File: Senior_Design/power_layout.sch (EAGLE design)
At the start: 110 parts, among them J1 AU-Y1008-2, J2 U.FL-R-SMT-1(01), J3 U.FL-R-SMT-1(01), T1 BCX70SMD, T2 BCX70SMD, U1 SIM7000E, U2 TUSB2046BVFR, U3 MAX3373EEKA+T, U4 TPS2044BDR, X1 332-04

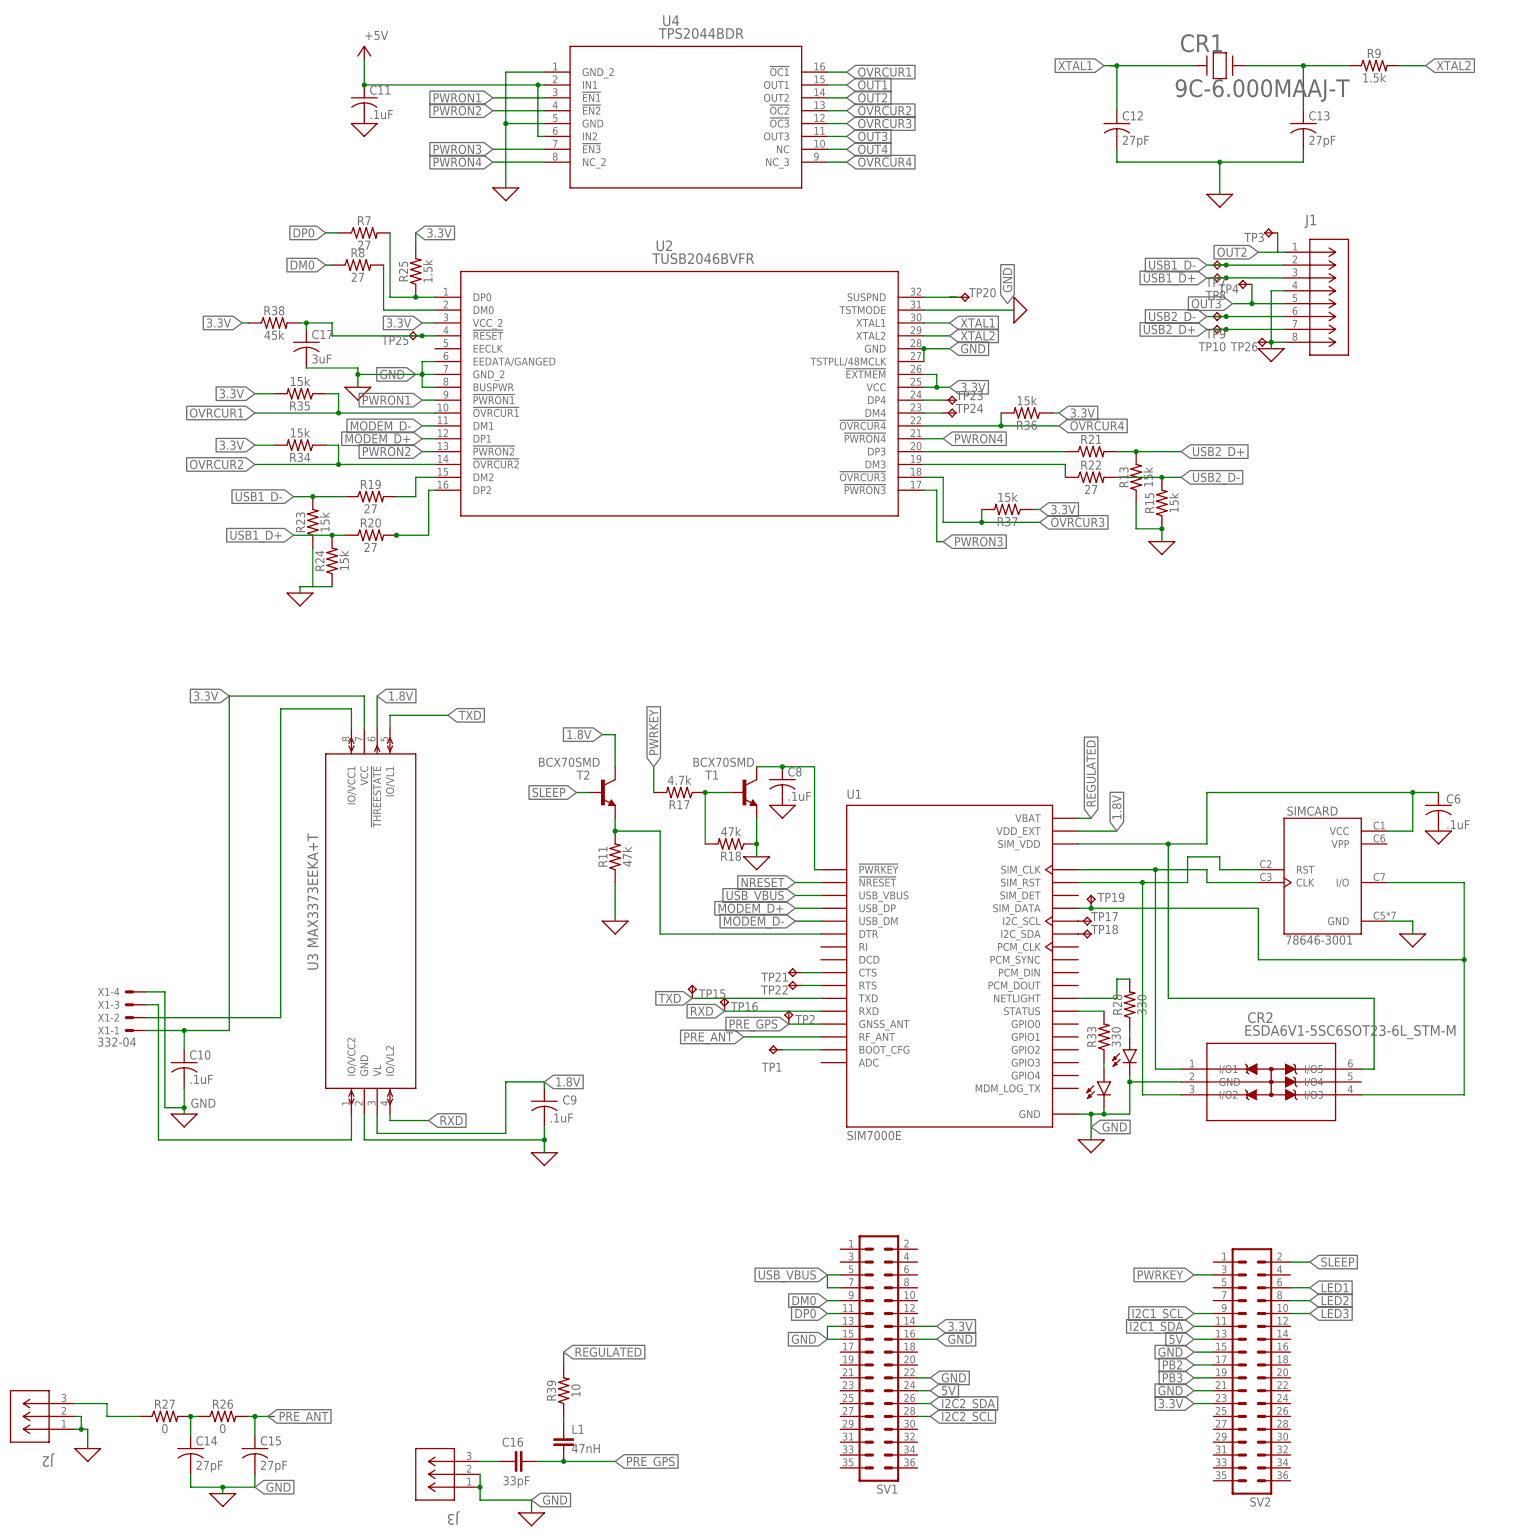
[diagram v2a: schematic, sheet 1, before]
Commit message: Add files via upload
This push includes the changes from Dr Pitts' Review and is THE Beta Board for purchasing.
-Cam files are processed in the folder "Beta Spin"
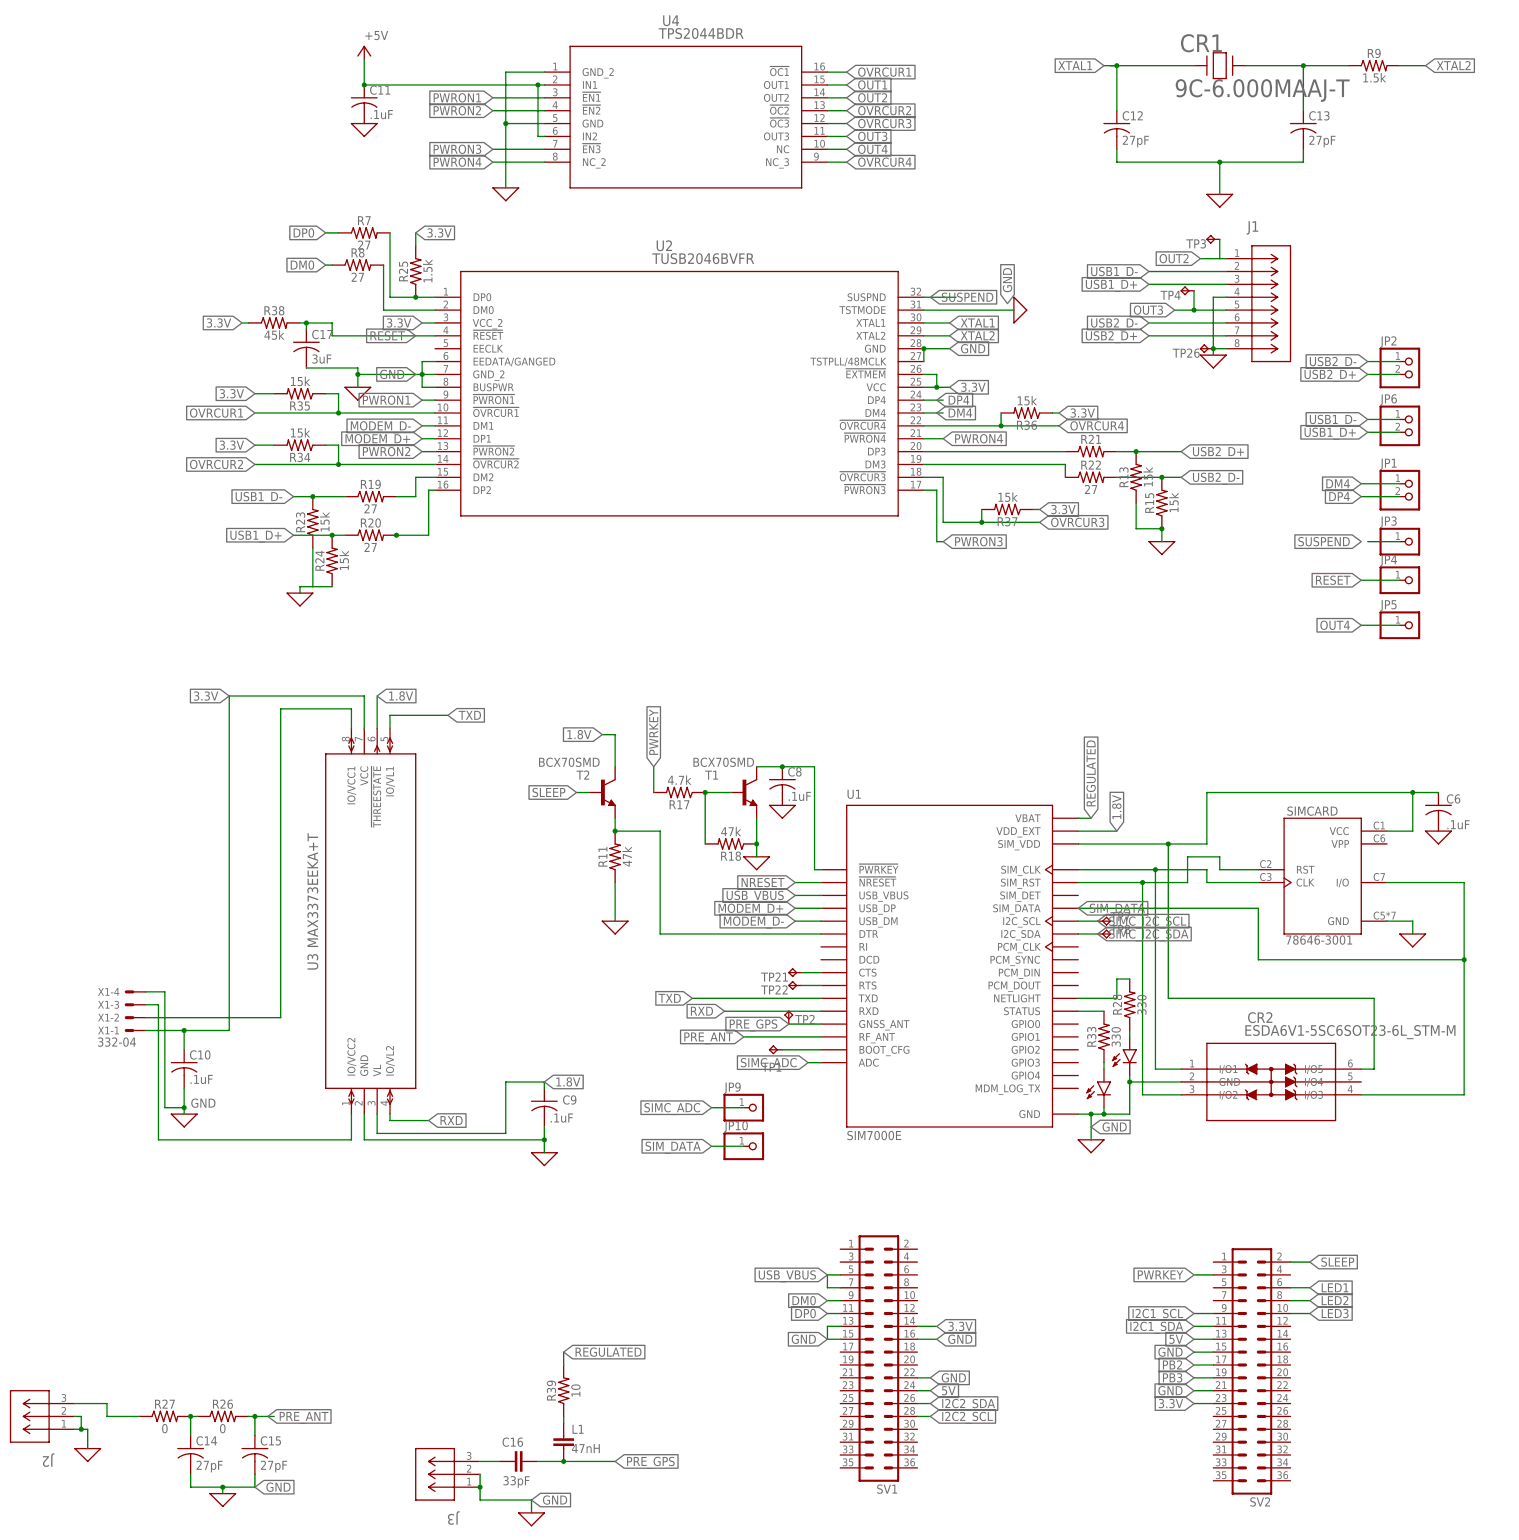
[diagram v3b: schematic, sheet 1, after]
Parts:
- removed TP10, TP11, TP12, TP13, TP14, TP15, TP16, TP17, TP18, TP19, TP20, TP23, TP24, TP25, TP9: TPTP10R, testpad:TPTP10R
- added JP1, JP2, JP6, JP7, JP8: (no value), pinhead:PINHD-1X2
- added JP10, JP3, JP4, JP5, JP9: (no value), pinhead:PINHD-1X1
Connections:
- removed net N$24: TP17.TP, U1.I2C_SCL
- removed net N$25: TP23.TP, U2.DP4
- removed net N$26: TP24.TP, U2.DM4
- removed net N$28: TP20.TP, U2.SUSPND
- removed net N$31: TP18.TP, U1.I2C_SDA
- removed net N$34: C17.1, R38.2, TP25.TP, U2.!RESET
- removed net N$6: CR2.I/O3, SIMCARD.I/O, TP19.TP, U1.SIM_DATA
- new net DM4: JP1.1, U2.DM4
- new net DP4: JP1.2, U2.DP4
- new net RESET: C17.1, JP4.1, R38.2, U2.!RESET
- new net SIMC_ADC: JP9.1, U1.ADC
- new net SIMC_I2C_SCL: TP7.TP, U1.I2C_SCL
- new net SIMC_I2C_SDA: TP8.TP, U1.I2C_SDA
- new net SIM_DATA: CR2.I/O3, JP10.1, SIMCARD.I/O, U1.SIM_DATA
- new net SUSPEND: JP3.1, U2.SUSPND
- net I2C1_SCL: now also JP8.1; no longer TP11.TP
- net I2C1_SDA: now also JP8.2; no longer TP12.TP
- net I2C2_SCL: now also JP7.1; no longer TP13.TP
- net I2C2_SDA: now also JP7.2; no longer TP14.TP
- net OUT4: now also JP5.1
- net RXD: no longer TP16.TP
- net TXD: no longer TP15.TP
- net USB1_D+: now also JP6.2; no longer TP8.TP
- net USB1_D-: now also JP6.1; no longer TP7.TP
- net USB2_D+: now also JP2.2; no longer TP10.TP
- net USB2_D-: now also JP2.1; no longer TP9.TP
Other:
- moved on the sheet: J1, TP26, TP3, TP4, TP7, TP8

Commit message: Adding Final Design Files
Incorporated all changes from Beta Assembly
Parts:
- removed TP27, TP28: TPTP10R, testpad:TPTP10R
- R6: value 470k -> 1500
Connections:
- net 0: now also RESET.2
- net 3.3V: now also R10.2; no longer RESET.1
- net GND: no longer R10.1, TP27.TP, TP28.TP
- net NRESET: now also R10.1, RESET.1; no longer R10.2, RESET.2
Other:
- note added: "Janak Patel Liza Chevalier Arthur Brazzle Alex Minser"
- note removed: "Janak Patel Liza Lance Arthur Brazzle Alex Minser"
- moved on the sheet: RESET
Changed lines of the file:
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@@
 <setting verticaltext="up"/>
 </settings>
-<grid distance="0.05" unitdist="inch" unit="inch" style="lines" multiple="1" display="no" altdistance="0.01" altunitdist="inch" altunit="inch"/>
+<grid distance="0.1" unitdist="inch" unit="inch" style="lines" multiple="1" display="no" altdistance="0.01" altunitdist="inch" altunit="inch"/>
 <layers>
 <layer number="1" name="Top" color="4" fill="1" visible="no" active="no"/>
@@
 <part name="R4" library="SparkFun-Resistors" library_urn="urn:adsk.eagle:library:532" deviceset="RESISTOR" device="0805" package3d_urn="urn:adsk.eagle:package:39651/1" value="47k"/>
 <part name="R5" library="SparkFun-Resistors" library_urn="urn:adsk.eagle:library:532" deviceset="RESISTOR" device="0805" package3d_urn="urn:adsk.eagle:package:39651/1" value="100k"/>
-<part name="R6" library="SparkFun-Resistors" library_urn="urn:adsk.eagle:library:532" deviceset="RESISTOR" device="0805" package3d_urn="urn:adsk.eagle:package:39651/1" value="470k"/>
+<part name="R6" library="SparkFun-Resistors" library_urn="urn:adsk.eagle:library:532" deviceset="RESISTOR" device="0805" package3d_urn="urn:adsk.eagle:package:39651/1" value="1500"/>
 <part name="X_14" library="ngspice-simulation" library_urn="urn:adsk.eagle:library:527439" deviceset="GND" device=""/>
 <part name="C2" library="rcl" library_urn="urn:adsk.eagle:library:334" deviceset="C-US" device="C0805" package3d_urn="urn:adsk.eagle:package:23617/2" value="0.1uF"/>
@@
 <part name="TP22" library="testpad" library_urn="urn:adsk.eagle:library:385" deviceset="TP" device="TP10R" package3d_urn="urn:adsk.eagle:package:27959/1" value="TPTP10R"/>
 <part name="TP26" library="testpad" library_urn="urn:adsk.eagle:library:385" deviceset="TP" device="TP10R" package3d_urn="urn:adsk.eagle:package:27959/1" value="TPTP10R"/>
-<part name="TP27" library="testpad" library_urn="urn:adsk.eagle:library:385" deviceset="TP" device="TP10R" package3d_urn="urn:adsk.eagle:package:27959/1" value="TPTP10R"/>
-<part name="TP28" library="testpad" library_urn="urn:adsk.eagle:library:385" deviceset="TP" device="TP10R" package3d_urn="urn:adsk.eagle:package:27959/1" value="TPTP10R"/>
 <part name="J3" library="Personal" deviceset="U.FL-R-SMT-1(01)" device=""/>
 <part name="L1" library="rcl" library_urn="urn:adsk.eagle:library:334" deviceset="C-EU" device="C1608" package3d_urn="urn:adsk.eagle:package:23621/2" value="47nH"/>
@@
 <text x="-68.58" y="-127" size="1.778" layer="112">NSCU ECE Senior Design 2020</text>
 <text x="-60.96" y="-137.16" size="1.778" layer="112">Janak Patel
-Liza Lance
+Liza Chevalier
 Arthur Brazzle
 Alex Minser</text>
@@
 <instance part="R2" gate="G$1" x="99.06" y="86.36" smashed="yes" rot="R90" grouprefs="USER_IO"/>
 <instance part="R3" gate="G$1" x="88.9" y="86.36" smashed="yes" rot="R90" grouprefs="USER_IO"/>
-<instance part="R10" gate="G$1" x="7.62" y="73.66" smashed="yes" rot="R90" grouprefs="USER_IO"/>
-<instance part="X_16" gate="G$1" x="7.62" y="68.58" smashed="yes" rot="MR0" grouprefs="USER_IO"/>
+<instance part="R10" gate="G$1" x="7.62" y="91.44" smashed="yes" rot="R90" grouprefs="USER_IO"/>
+<instance part="X_16" gate="G$1" x="7.62" y="66.04" smashed="yes" rot="MR0" grouprefs="USER_IO"/>
 <instance part="R14" gate="G$1" x="33.02" y="73.66" smashed="yes" rot="R90" grouprefs="USER_IO"/>
 <instance part="X_24" gate="G$1" x="33.02" y="68.58" smashed="yes" rot="MR0" grouprefs="USER_IO"/>
@@
 <instance part="R31" gate="G$1" x="166.37" y="104.14" smashed="yes" rot="R180"/>
 <instance part="R32" gate="G$1" x="166.37" y="96.52" smashed="yes" rot="R180"/>
-<instance part="TP27" gate="G$1" x="130.81" y="71.12" smashed="yes" rot="R90">
-<attribute name="NAME" x="130.81" y="71.12" size="1.778" layer="95" rot="R180"/>
-<attribute name="TP_SIGNAL_NAME" x="132.08" y="72.39" size="1.778" layer="97" rot="R90"/>
-</instance>
-<instance part="TP28" gate="G$1" x="166.37" y="71.12" smashed="yes" rot="R90">
-<attribute name="NAME" x="166.37" y="71.12" size="1.778" layer="95" rot="R180"/>
-<attribute name="TP_SIGNAL_NAME" x="167.64" y="72.39" size="1.778" layer="97" rot="R90"/>
-</instance>
-<instance part="RESET" gate="A" x="7.62" y="88.9" smashed="yes" rot="R270">
-<attribute name="NAME" x="9.7028" y="96.7994" size="3.4798" layer="95" ratio="10" rot="SR270"/>
-<attribute name="NAME" x="9.7028" y="96.7994" size="3.4798" layer="95" ratio="10" rot="SR270"/>
+<instance part="RESET" gate="A" x="7.62" y="73.66" smashed="yes" rot="R270">
+<attribute name="NAME" x="9.7028" y="81.5594" size="3.4798" layer="95" ratio="10" rot="SR270"/>
+<attribute name="NAME" x="9.7028" y="81.5594" size="3.4798" layer="95" ratio="10" rot="SR270"/>
 </instance>
 <instance part="BTN2" gate="A" x="33.02" y="88.9" smashed="yes" rot="R270">
@@
 </segment>
 <segment>
-<pinref part="R10" gate="G$1" pin="1"/>
-<pinref part="X_16" gate="G$1" pin="0"/>
-</segment>
-<segment>
 <pinref part="R14" gate="G$1" pin="1"/>
 <pinref part="X_24" gate="G$1" pin="0"/>
@@
 <wire x1="133.35" y1="71.12" x2="133.35" y2="68.58" width="0.1524" layer="91" grouprefs="GROVE"/>
 <pinref part="X_14" gate="G$1" pin="0"/>
-<pinref part="TP27" gate="G$1" pin="TP"/>
-<junction x="133.35" y="71.12"/>
 </segment>
 <segment>
@@
 <wire x1="168.91" y1="71.12" x2="168.91" y2="68.58" width="0.1524" layer="91" grouprefs="GROVE"/>
 <pinref part="X_22" gate="G$1" pin="0"/>
-<pinref part="TP28" gate="G$1" pin="TP"/>
-<junction x="168.91" y="71.12"/>
 </segment>
 <segment>
@@
 </segment>
 </net>
-<net name="NRESET" class="0">
-<segment>
-<pinref part="R10" gate="G$1" pin="2"/>
-<wire x1="7.62" y1="81.28" x2="7.62" y2="78.74" width="0.1524" layer="91" grouprefs="USER_IO"/>
-<wire x1="7.62" y1="81.28" x2="15.24" y2="81.28" width="0.1524" layer="91" grouprefs="USER_IO"/>
-<label x="15.24" y="81.28" size="1.778" layer="95" xref="yes" grouprefs="USER_IO"/>
-<pinref part="RESET" gate="A" pin="2"/>
-<junction x="7.62" y="81.28"/>
-</segment>
-</net>
 <net name="3.3V" class="1">
 <segment>
@@
 </segment>
 <segment>
-<wire x1="7.62" y1="96.52" x2="7.62" y2="106.68" width="0.1524" layer="91"/>
-<label x="7.62" y="106.68" size="1.778" layer="95" xref="yes"/>
-<pinref part="RESET" gate="A" pin="1"/>
-</segment>
-<segment>
 <wire x1="33.02" y1="96.52" x2="33.02" y2="106.68" width="0.1524" layer="91"/>
 <label x="33.02" y="106.68" size="1.778" layer="95" xref="yes"/>
@@
 <label x="55.88" y="106.68" size="1.778" layer="95" xref="yes"/>
 <pinref part="BTN3" gate="A" pin="1"/>
+</segment>
+<segment>
+<pinref part="R10" gate="G$1" pin="2"/>
+<wire x1="7.62" y1="96.52" x2="7.62" y2="106.68" width="0.1524" layer="91"/>
+<label x="7.62" y="106.68" size="1.778" layer="95" xref="yes"/>
 </segment>
 </net>
@@
 </segment>
 </net>
+<net name="NRESET" class="0">
+<segment>
+<pinref part="R10" gate="G$1" pin="1"/>
+<pinref part="RESET" gate="A" pin="1"/>
+<wire x1="7.62" y1="86.36" x2="7.62" y2="83.82" width="0.1524" layer="91"/>
+<label x="10.16" y="83.82" size="1.778" layer="95" xref="yes"/>
+<wire x1="7.62" y1="83.82" x2="7.62" y2="81.28" width="0.1524" layer="91"/>
+<wire x1="7.62" y1="83.82" x2="10.16" y2="83.82" width="0.1524" layer="91"/>
+<junction x="7.62" y="83.82"/>
+</segment>
+</net>
+<net name="0" class="0">
+<segment>
+<pinref part="RESET" gate="A" pin="2"/>
+<pinref part="X_16" gate="G$1" pin="0"/>
+</segment>
+</net>
